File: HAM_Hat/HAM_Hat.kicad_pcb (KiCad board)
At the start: 2 copper layers, 65 x 56.5 mm, 56 parts, among them J101 TL212V-02P-G12S, J102 DB-9RS-C, J103 NCW254-02S, J104 U.FL-R-SMT-1(80), J105 NCW200S-04R, J3 FHDH2.54-40, M101 Fan, Q101 BSS138, Q102 BSS138, Q103 BSS138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

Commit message: Bump version: 2.0.0 → 2.0.1
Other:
- board text added: "v2.0.1"
- board text removed: "v2.0.0"
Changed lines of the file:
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@@
 		(title "Ham hat")
 		(date "2021-12-03")
-		(rev "v2.0.0")
+		(rev "v2.0.1")
 		(company "Logonex Bt.")
 		(comment 1 "Drawn by HA5OGL")
@@
 		)
 	)
-	(gr_text "v2.0.0"
+	(gr_text "v2.0.1"
 		(at 153.7 78.1 0)
 		(layer "F.SilkS")

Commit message: Add DCD LED
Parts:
- added D106: GRE, LED_SMD:LED_0603_1608Metric, F.Cu at (152.1, 77.8)
- added R114: 510R, Resistor_SMD:R_0603_1608Metric, F.Cu at (155.8, 77.8)
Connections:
- J3 pad 11: /PTT -> unconnected-(J3-BCM17-Pad11)
- J3 pad 32: unconnected-(J3-BCM12-Pad32) -> /PTT
- J3 pad 36: unconnected-(J3-BCM16-Pad36) -> /DCD
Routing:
- net /PTT: track 24.4 -> 52.8 mm
- net /DCD: track 0.00 -> 18.1 mm
- net Net-(D106-A): track 0.00 -> 2.09 mm
- net GND: track 10.1 -> 9.93 mm, vias 139 -> 137
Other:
- board text added: "CD"
- board text added: "CW"
- board text added: "TX"

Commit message: Bump version: 2.0.1 → 2.1.0
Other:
- board text added: "v2.1.0"
- board text removed: "v2.0.1"
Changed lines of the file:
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@@
 		(title "Ham hat")
 		(date "2021-12-03")
-		(rev "v2.0.1")
+		(rev "v2.1.0")
 		(company "Logonex Bt.")
 		(comment 1 "Drawn by HA5OGL")
@@
 		)
 	)
-	(gr_text "v2.0.1"
+	(gr_text "v2.1.0"
 		(at 142.8 81.2 0)
 		(layer "F.SilkS")

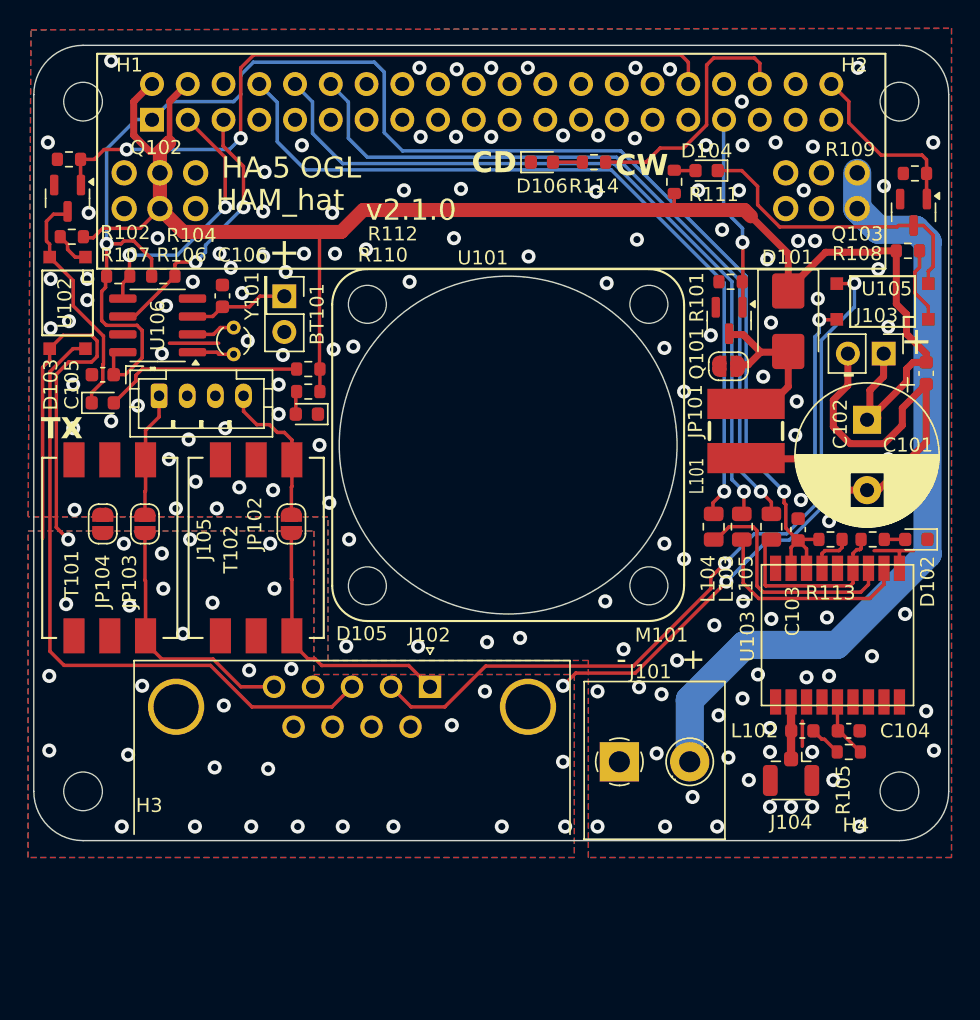
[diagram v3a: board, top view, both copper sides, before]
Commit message: LED moved
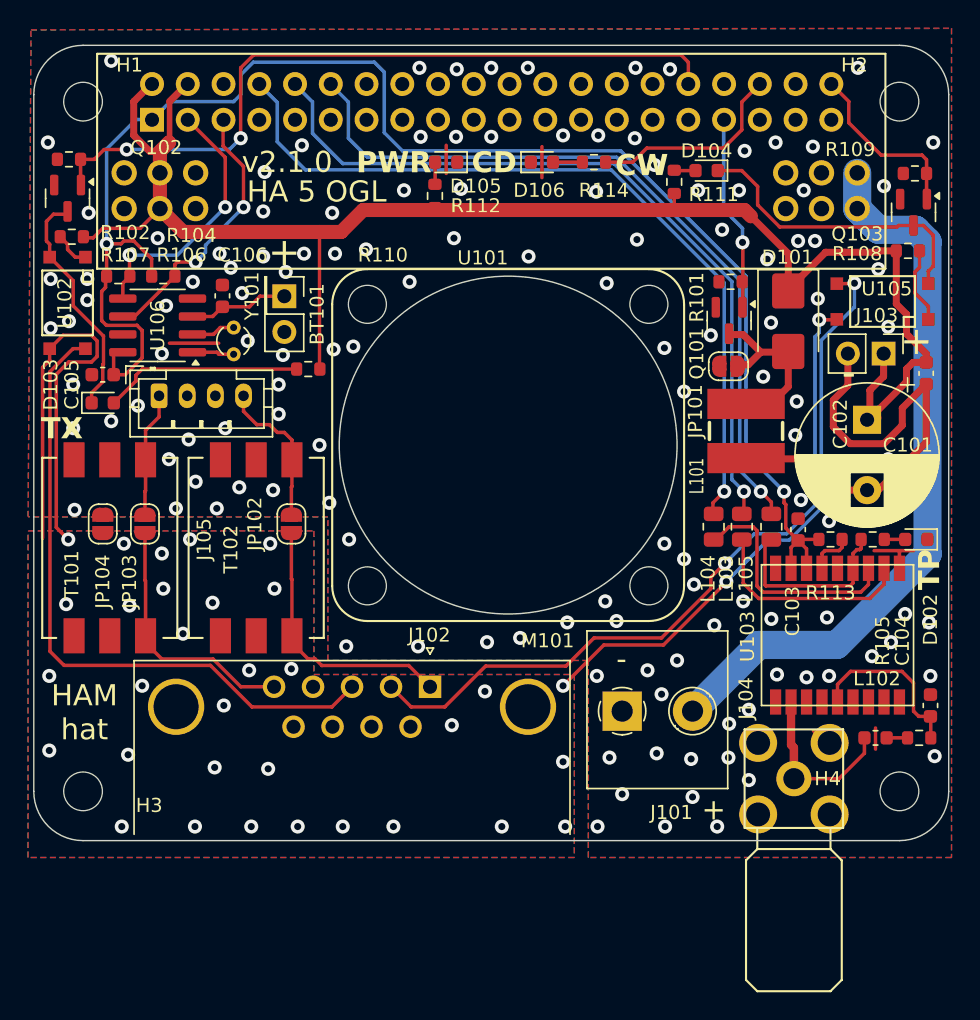
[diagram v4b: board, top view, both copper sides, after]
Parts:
- J104: value U.FL-R-SMT-1(80) -> SMA6252A2; footprint Connector_Coaxial:U.FL_Hirose_U.FL-R-SMT-1_Vertical -> l_rf:SMA_angled
- moved D105 20.5 mm to (145.3, 77.8)
- moved R112 16.6 mm to (144.5, 80.2), turned to -90 degrees
- moved C104 6.07 mm to (179.7, 116.4), turned to -90 degrees
- moved L102 5.22 mm to (175.8, 118.7)
- moved R105 5.10 mm to (178.9, 118.7)
- moved J101 3.61 mm to (157.8, 116.8)
- moved J104 0.40 mm to (170.0, 121.6)
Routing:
- net Net-(J104-In): track 3.95 -> 12.4 mm
- net Net-(U103-VCC_RF): track 4.28 -> 12.5 mm
- net GND: track 9.93 -> 16.3 mm, vias 137 -> 135
- net Net-(J101-Pin_2): track 56.3 -> 52.0 mm
- net /DCD: track 18.1 -> 14.4 mm
- net /P5V_HAT: track 114.4 -> 112.8 mm
- net Net-(L102-Pad1): track 2.31 -> 1.49 mm
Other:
- board text added: "HAM hat"
- board text added: "PWR"
- board text added: "TP"
- board text removed: "HAM_hat"

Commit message: Alternative LED positions
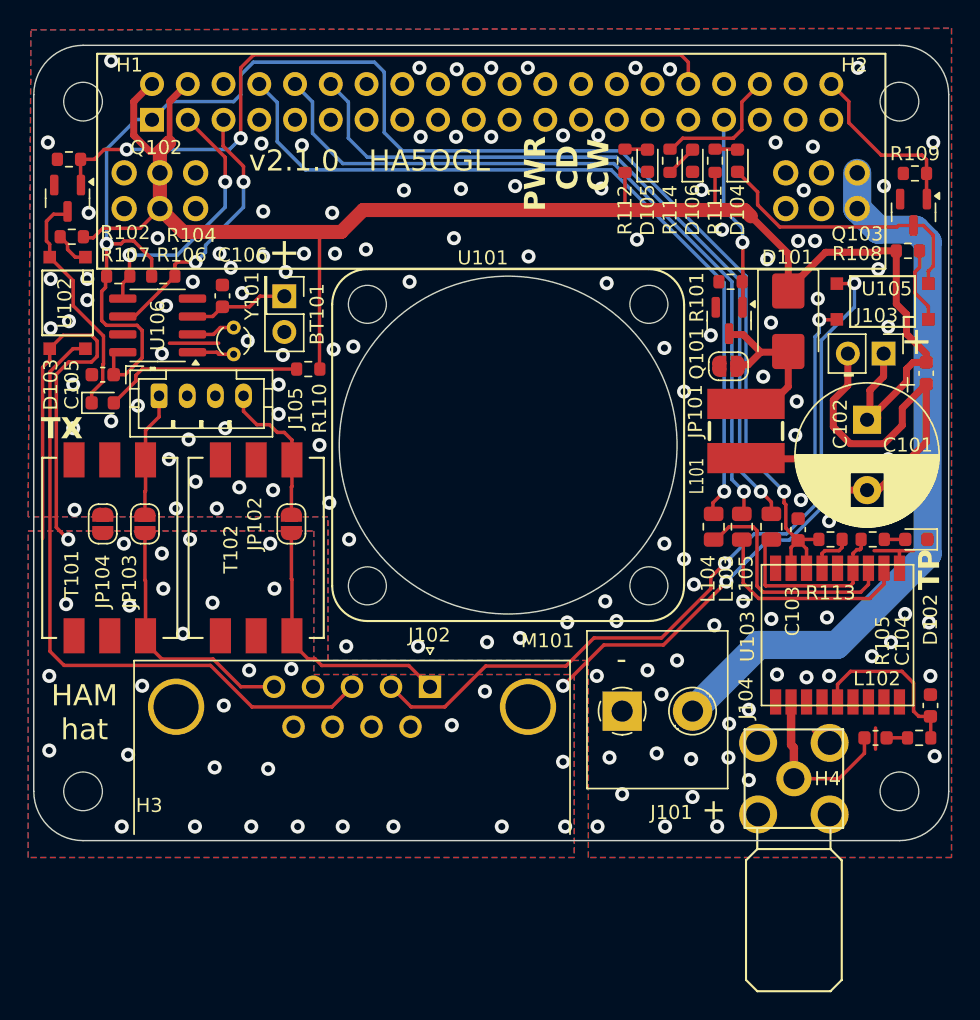
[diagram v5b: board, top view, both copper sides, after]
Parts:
- moved D105 14.3 mm to (159.6, 77.7), turned to 90 degrees
- moved R112 13.7 mm to (158.0, 77.7)
- moved D106 10.7 mm to (162.8, 77.7), turned to 90 degrees
- moved R114 5.40 mm to (161.2, 77.7), turned to -90 degrees
- moved R111 3.26 mm to (164.4, 77.7)
- moved D104 2.31 mm to (166.0, 77.7), turned to 90 degrees
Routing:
- net /DCD: track 14.4 -> 9.52 mm
- net GND: track 16.3 -> 12.1 mm, vias 135 -> 132
- net /P5V_HAT: track 112.8 -> 116.9 mm
- net Net-(D104-K): track 21.9 -> 20.2 mm
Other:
- board text added: "HA5OGL"
- board text removed: "HA 5 OGL"

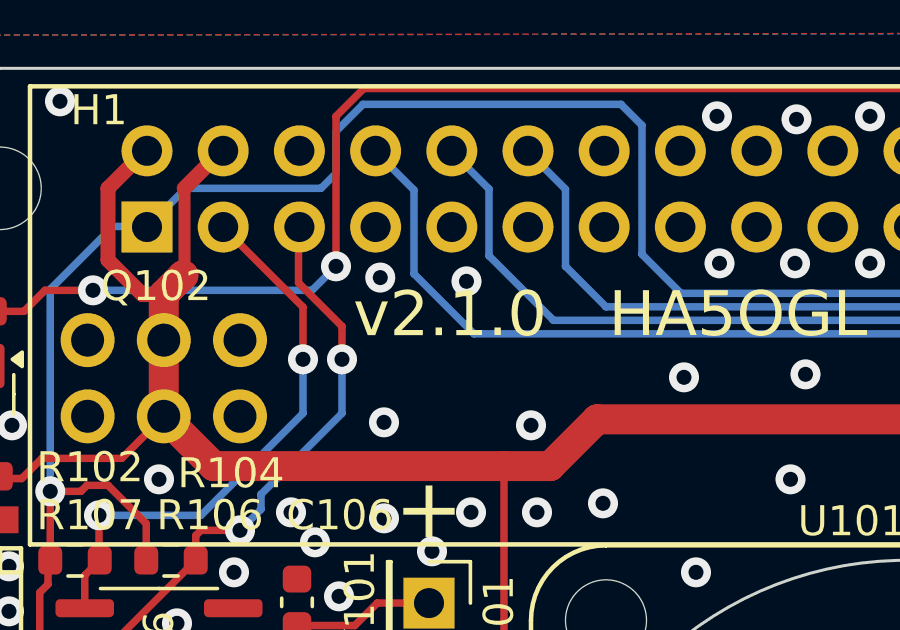
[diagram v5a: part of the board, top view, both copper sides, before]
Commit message: Bump version: 2.1.0 → 2.1.1
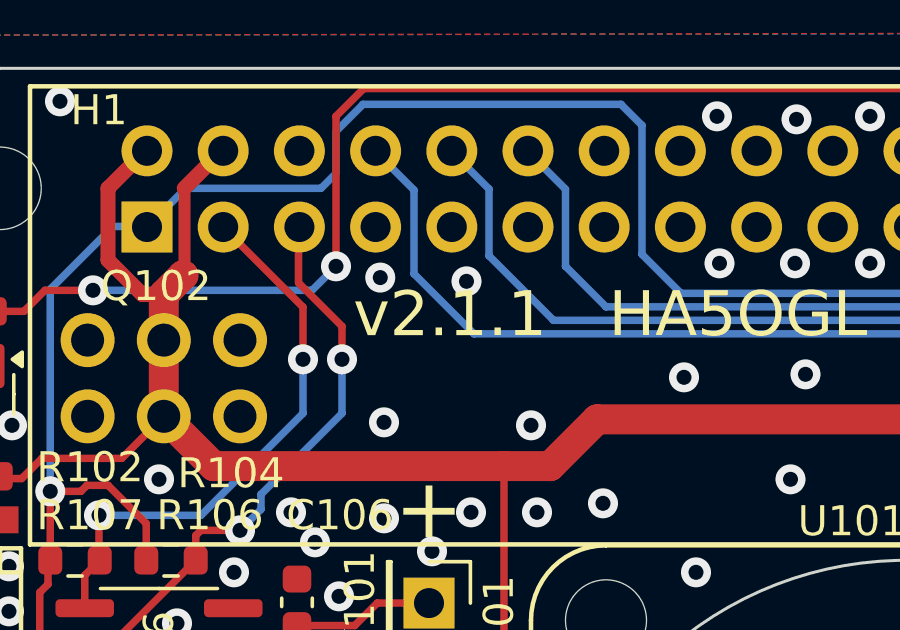
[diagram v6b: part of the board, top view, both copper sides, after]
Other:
- board text added: "v2.1.1"
- board text removed: "v2.1.0"
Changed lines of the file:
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@@
 		(title "Ham hat")
 		(date "2025-04-30")
-		(rev "v2.1.0")
+		(rev "v2.1.1")
 		(company "Logonex Bt.")
 		(comment 1 "Drawn by HA5OGL")
@@
 		)
 	)
-	(gr_text "v2.1.0"
+	(gr_text "v2.1.1"
 		(at 134.5 77.7 0)
 		(layer "F.SilkS")

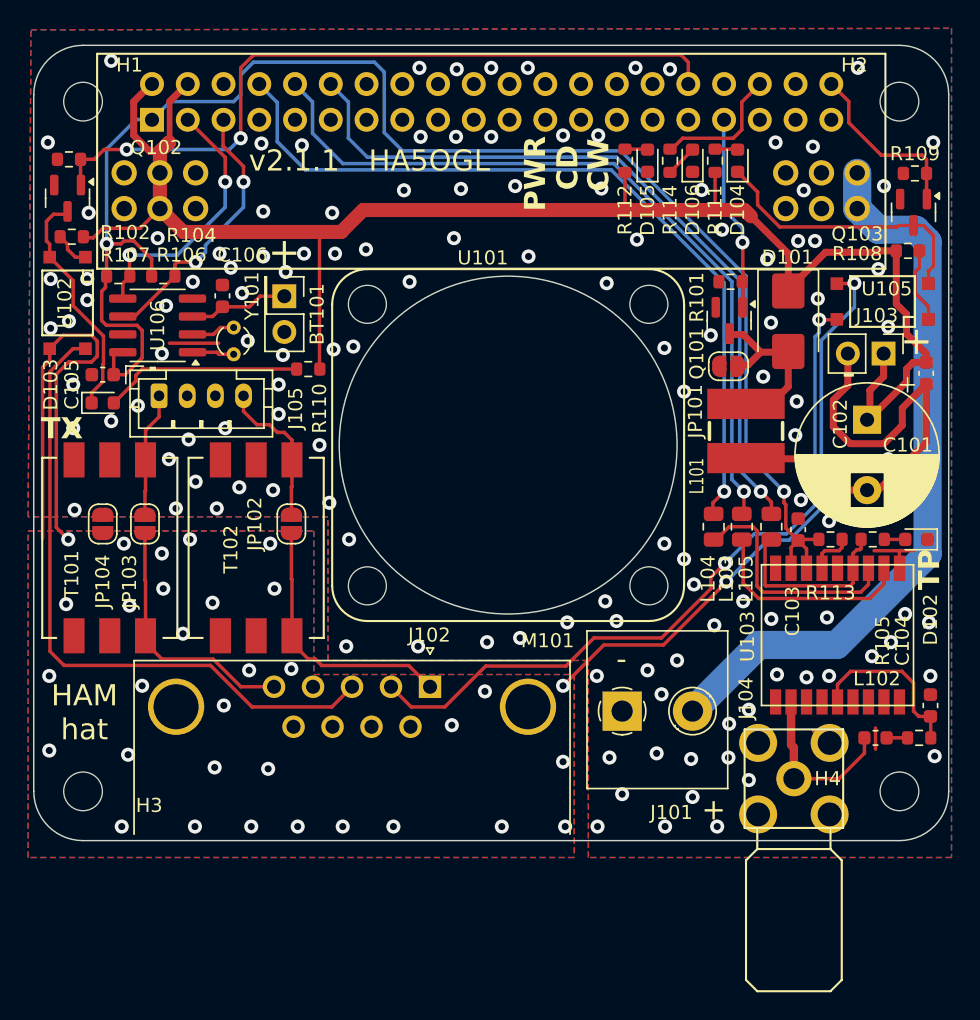
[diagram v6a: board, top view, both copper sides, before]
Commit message: Add shutdown switch interface
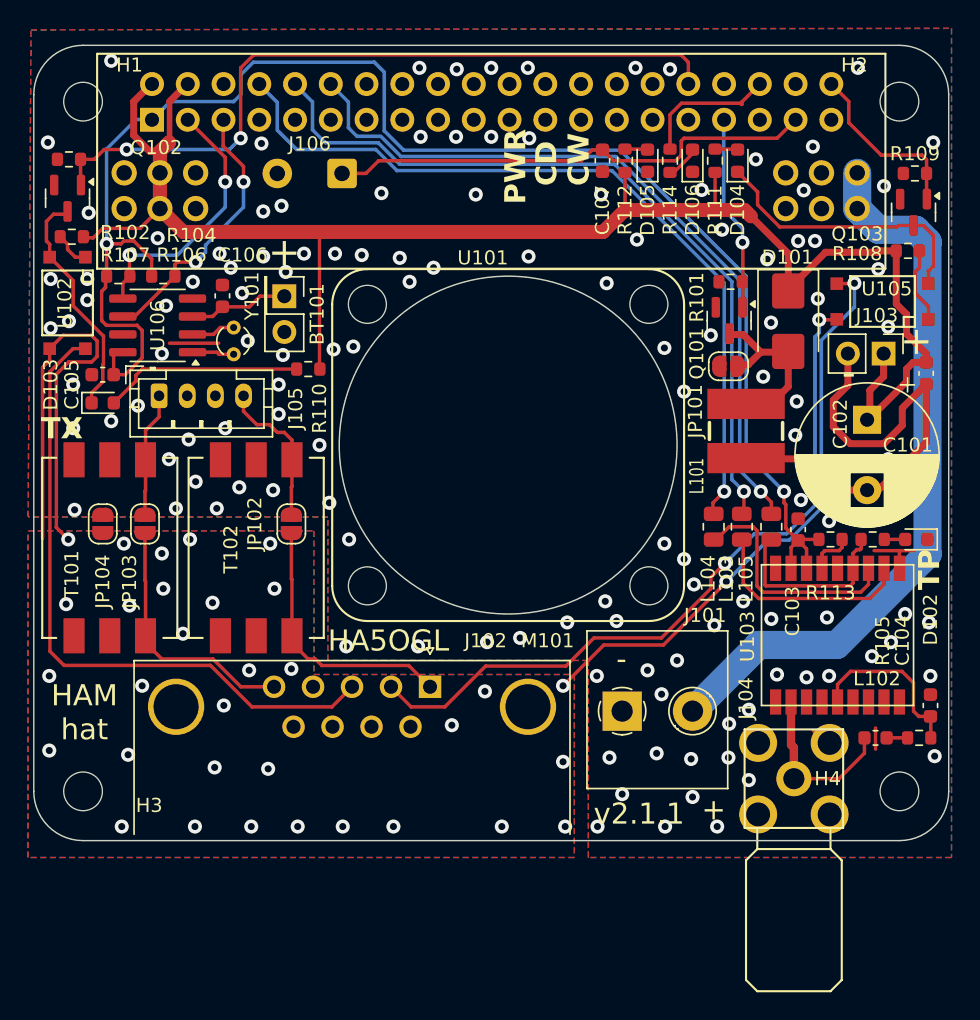
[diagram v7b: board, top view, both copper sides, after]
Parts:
- added C107: 100n, Capacitor_SMD:C_0603_1608Metric, F.Cu at (156.4, 77.7)
- added J106: Conn_01x02, Connector_Wire:SolderWire-0.5sqmm_1x02_P4.6mm_D0.9mm_OD2.1mm, F.Cu at (137.9, 78.6)
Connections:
- J3 pad 37: unconnected-(J3-BCM26-Pad37) -> /SHUTDOWN
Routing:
- net /SHUTDOWN: track 0.00 -> 35.0 mm
- net GND: vias 132 -> 130

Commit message: Add run LED
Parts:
- added D107: RED, LED_SMD:LED_0603_1608Metric, F.Cu at (156.4, 77.7)
- added R115: 510R, Resistor_SMD:R_0603_1608Metric, F.Cu at (154.8, 77.7)
- moved C107 3.20 mm to (153.2, 77.7), turned to 90 degrees
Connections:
- J3 pad 26: unconnected-(J3-BCM7-Pad26) -> /RUN_LED
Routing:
- net /RUN_LED: track 0.00 -> 5.65 mm
- net /SHUTDOWN: track 35.0 -> 38.6 mm
- net Net-(D107-A): track 0.00 -> 2.28 mm
- net GND: vias 130 -> 134
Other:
- board text added: "RUN"
